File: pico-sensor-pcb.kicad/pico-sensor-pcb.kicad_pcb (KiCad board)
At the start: 2 copper layers, 46 x 60 mm, 38 parts, among them J1 Conn_PDM, J10 Conn_PCB_2, J11 Conn_I2C1, J13 Conn_I2C1, J2 Conn_RUN_ON, J3 Conn_Controls, J7 Conn_PCB_1, SW1 SW_Push, SW2 SW_Push, SW3 SW_Push, SW4 SW_Push, SW5 SW_Push, U1 AHT20, U2 BH1750FVI-TR, U3 SCD40_Breakout, U4 ENS160_Breakout

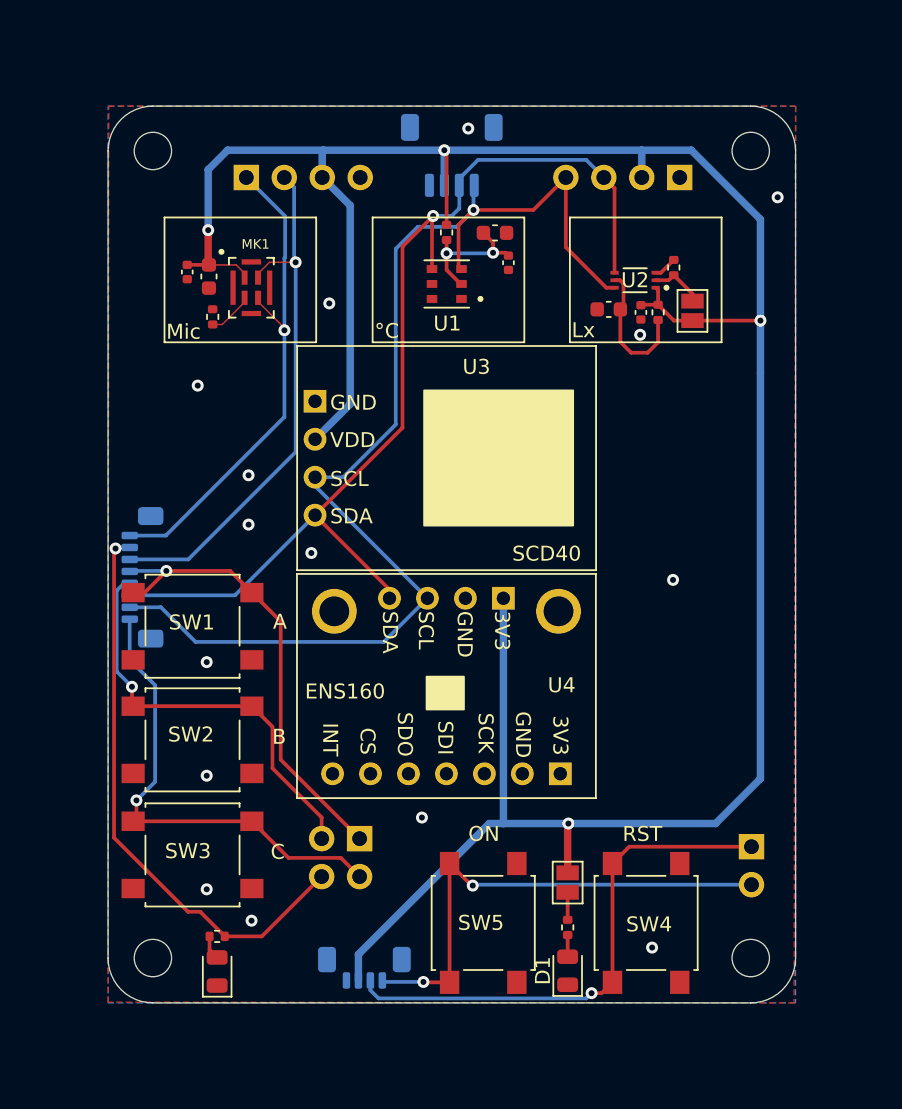
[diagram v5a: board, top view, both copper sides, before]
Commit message: Sensor-PCB Rev 1.95: larger PCB, I2C-pullups, labels (ready for review)
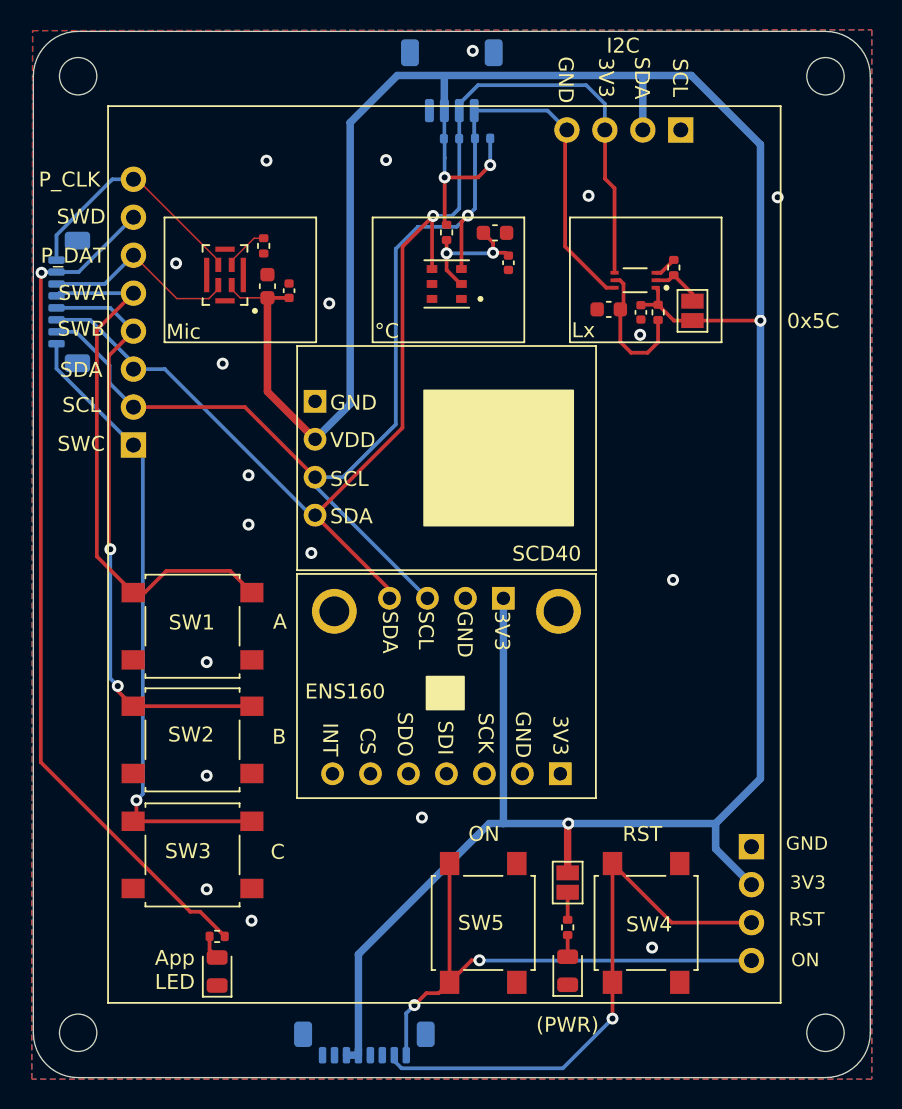
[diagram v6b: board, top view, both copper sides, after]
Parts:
- removed J3: Conn_Controls, Connector_PinHeader_2.54mm:PinHeader_2x02_P2.54mm_Vertical
- added R7: 10K, Resistor_SMD:R_0402_1005Metric, B.Cu at (125.1, 102.2)
- added R8: 10K, Resistor_SMD:R_0402_1005Metric, B.Cu at (123.0, 102.2)
- J1: value Conn_PDM -> THT_PCB2; footprint Connector_PinHeader_2.54mm:PinHeader_1x04_P2.54mm_Vertical -> Connector_PinHeader_2.54mm:PinHeader_1x08_P2.54mm_Vertical
- J10: value Conn_PCB_2 -> Conn_PCB2
- J2: footprint Connector_PinHeader_2.54mm:PinHeader_1x02_P2.54mm_Vertical -> Connector_PinHeader_2.54mm:PinHeader_1x04_P2.54mm_Vertical
- J7: footprint Connector_JST:JST_SUR_BM04B-SURS-TF_1x04-1MP_P0.80mm_Vertical -> Connector_JST:JST_SUR_BM08B-SURS-TF_1x08-1MP_P0.80mm_Vertical
- R5: value 150Ω -> 1K
- moved J1 19.4 mm to (101.7, 122.7), turned to 0 degrees
- moved J10 19.1 mm to (97.4, 113.1)
- moved H1 7.07 mm to (98.0, 98.0)
- moved H2 7.07 mm to (148.0, 98.0)
- moved H3 7.07 mm to (98.0, 162.0)
- moved H4 7.07 mm to (148.0, 162.0)
- moved C3 6.93 mm to (112.1, 112.3), turned to 90 degrees
- moved R2 5.85 mm to (110.4, 109.3), turned to 90 degrees
- moved J11 5.00 mm to (123.0, 98.3)
- moved J7 5.00 mm to (117.2, 162.7)
- moved C4 3.97 mm to (110.7, 112.0), turned to 90 degrees
- moved J13 3.18 mm to (138.3, 101.6)
- moved MK1 1.96 mm to (107.8, 111.3), turned to 180 degrees
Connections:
- J1 pad 1: /PDM_CLK -> /SWC
- J1 pad 2: /PDM_DAT -> /SCL
- J1 pad 3: +3V3 -> /SDA
- J1 pad 4: GND -> /SWB
- J2 pad 1: /RUN -> GND
- J2 pad 2: /~{ON} -> +3V3
- J7 pad 3: +3V3 -> unconnected-(J7-Pad3)
- J7 pad 4: GND -> unconnected-(J7-Pad4)
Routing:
- net /PDM_DAT: track 35.9 -> 13.0 mm, vias 1 -> 0
- net +3V3: track 179.6 -> 201.4 mm
- net /SWD: track 38.7 -> 57.6 mm
- net /SDA: track 70.4 -> 88.3 mm
- net /PDM_CLK: track 33.7 -> 16.3 mm, vias 1 -> 0
- net /SWB: track 28.0 -> 40.2 mm, vias 1 -> 2
- net /SWC: track 31.5 -> 42.6 mm
- net /SCL: track 80.4 -> 87.6 mm
- net /SWA: track 31.1 -> 36.4 mm, vias 1 -> 0
- net /RUN: track 35.2 -> 37.9 mm
- net /~{ON}: track 33.3 -> 35.3 mm
- net GND: track 1.57 -> 1.86 mm, vias 15 -> 19
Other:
- board size 46 x 60 mm -> 56 x 70 mm
- board text added: "(PWR)"
- board text added: "0x5C"
- board text added: "App LED"
- board text added: "I2C"
- board text added: "P_CLK"
- board text added: "P_DAT"
- board text added: "SWA"
- board text added: "SWB"
- board text added: "SWC"
- board text added: "SWD"
- board text added: "https://github.com/bablokb/pcb-pico-datalogger https://opendeved.net/ilce Rev 1.95"
- board text removed: "D"
- board text removed: "https://github.com/bablokb/pcb-pico-datalogger https://opendeved.net/ilce Rev 0.90"

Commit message: Sensor-PCB Rev 2.00: bump version to 2.00 (ready for production)
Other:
- board text added: "https://github.com/bablokb/pcb-pico-datalogger https://opendeved.net/ilce Rev 2.00"
- board text removed: "https://github.com/bablokb/pcb-pico-datalogger https://opendeved.net/ilce Rev 1.95"
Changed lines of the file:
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@@
     (property "Sheetname" "")
     (property "exclude_from_bom" "")
-    (attr through_hole exclude_from_bom)
+    (attr through_hole exclude_from_pos_files exclude_from_bom)
     (fp_text reference "J1" (at 0 2.33) (layer "B.SilkS") hide
       (effects (font (size 1 1) (thickness 0.15)) (justify mirror))
@@
     (property "Sheetname" "")
     (property "exclude_from_bom" "")
-    (attr through_hole exclude_from_bom)
+    (attr through_hole exclude_from_pos_files exclude_from_bom)
     (fp_text reference "J2" (at 0 2.33) (layer "B.SilkS") hide
       (effects (font (size 1 1) (thickness 0.15)) (justify mirror))
@@
     (pad "8" smd roundrect (at 2.8 -0.85 180) (size 0.5 1.1) (layers "B.Cu" "B.Paste" "B.Mask") (roundrect_rratio 0.25)
       (net 1 "GND") (pinfunction "Pin_8") (pintype "passive"))
-    (pad "MP" smd roundrect (at 4.1 0.55 180) (size 1.2 1.7) (layers "B.Cu" "B.Paste" "B.Mask") (roundrect_rratio 0.208333))
-    (pad "MP" smd roundrect (at -4.1 0.55 180) (size 1.2 1.7) (layers "B.Cu" "B.Paste" "B.Mask") (roundrect_rratio 0.208333))
+    (pad "MP" smd roundrect (at 4.1 0.55 180) (size 1.2 1.7) (layers "B.Cu" "B.Paste" "B.Mask") (roundrect_rratio 0.2083333333))
+    (pad "MP" smd roundrect (at -4.1 0.55 180) (size 1.2 1.7) (layers "B.Cu" "B.Paste" "B.Mask") (roundrect_rratio 0.2083333333))
     (model "${KICAD6_3DMODEL_DIR}/Connector_JST.3dshapes/JST_SUR_BM08B-SURS-TF_1x08-1MP_P0.80mm_Vertical.wrl"
       (offset (xyz 0 0 0))
@@
       (effects (font (size 1 1) (thickness 0.15)) (justify mirror))
     )
+    (fp_line (start 3.11 1.785) (end 2.06 1.785) (layer "B.SilkS") (width 0.12))
+    (fp_line (start -2.06 1.785) (end -2.06 2.775) (layer "B.SilkS") (width 0.12))
+    (fp_line (start -3.11 1.785) (end -2.06 1.785) (layer "B.SilkS") (width 0.12))
+    (fp_line (start 3.11 -0.715) (end 3.11 1.785) (layer "B.SilkS") (width 0.12))
+    (fp_line (start -3.11 -0.715) (end -3.11 1.785) (layer "B.SilkS") (width 0.12))
     (fp_line (start -1.94 -2.685) (end 1.94 -2.685) (layer "B.SilkS") (width 0.12))
-    (fp_line (start 3.11 -0.715) (end 3.11 1.785) (layer "B.SilkS") (width 0.12))
-    (fp_line (start -2.06 1.785) (end -2.06 2.775) (layer "B.SilkS") (width 0.12))
-    (fp_line (start -3.11 -0.715) (end -3.11 1.785) (layer "B.SilkS") (width 0.12))
-    (fp_line (start -3.11 1.785) (end -2.06 1.785) (layer "B.SilkS") (width 0.12))
-    (fp_line (start 3.11 1.785) (end 2.06 1.785) (layer "B.SilkS") (width 0.12))
+    (fp_line (start -3.9 3.28) (end -3.9 -3.28) (layer "B.CrtYd") (width 0.05))
     (fp_line (start -3.9 -3.28) (end 3.9 -3.28) (layer "B.CrtYd") (width 0.05))
     (fp_line (start 3.9 3.28) (end -3.9 3.28) (layer "B.CrtYd") (width 0.05))
     (fp_line (start 3.9 -3.28) (end 3.9 3.28) (layer "B.CrtYd") (width 0.05))
-    (fp_line (start -3.9 3.28) (end -3.9 -3.28) (layer "B.CrtYd") (width 0.05))
-    (fp_line (start -3 -2.575) (end 3 -2.575) (layer "B.Fab") (width 0.1))
-    (fp_line (start 3 1.675) (end 3 -2.575) (layer "B.Fab") (width 0.1))
     (fp_line (start -2 1.675) (end -1.5 0.967893) (layer "B.Fab") (width 0.1))
-    (fp_line (start -3 1.675) (end -3 -2.575) (layer "B.Fab") (width 0.1))
     (fp_line (start -3 1.675) (end 3 1.675) (layer "B.Fab") (width 0.1))
     (fp_line (start -1.5 0.967893) (end -1 1.675) (layer "B.Fab") (width 0.1))
+    (fp_line (start -3 1.675) (end -3 -2.575) (layer "B.Fab") (width 0.1))
+    (fp_line (start 3 1.675) (end 3 -2.575) (layer "B.Fab") (width 0.1))
+    (fp_line (start -3 -2.575) (end 3 -2.575) (layer "B.Fab") (width 0.1))
     (pad "1" smd roundrect (at -1.5 2) (size 0.6 1.55) (layers "B.Cu" "B.Paste" "B.Mask") (roundrect_rratio 0.25)
       (net 1 "GND") (pinfunction "GND") (pintype "power_in"))
@@
     (pad "4" smd roundrect (at 1.5 2) (size 0.6 1.55) (layers "B.Cu" "B.Paste" "B.Mask") (roundrect_rratio 0.25)
       (net 3 "/SCL") (pinfunction "SCL") (pintype "bidirectional"))
+    (pad "MP" smd roundrect (at -2.8 -1.875) (size 1.2 1.8) (layers "B.Cu" "B.Paste" "B.Mask") (roundrect_rratio 0.2083333333))
     (pad "MP" smd roundrect (at 2.8 -1.875) (size 1.2 1.8) (layers "B.Cu" "B.Paste" "B.Mask") (roundrect_rratio 0.2083333333))
-    (pad "MP" smd roundrect (at -2.8 -1.875) (size 1.2 1.8) (layers "B.Cu" "B.Paste" "B.Mask") (roundrect_rratio 0.2083333333))
     (model "${KICAD6_3DMODEL_DIR}/Connector_JST.3dshapes/JST_SH_SM04B-SRSS-TB_1x04-1MP_P1.00mm_Horizontal.wrl"
       (offset (xyz 0 0 0))
       (scale (xyz 1 1 1))
       (rotate (xyz 0 0 0))
+    )
+    (model "/home/bablokb/kicad/SM04B-SRSS-TB.step"
+      (offset (xyz 0 1.35 -0.35))
+      (scale (xyz 1 1 1))
+      (rotate (xyz -90 0 0))
     )
   )
@@
     (effects (font (size 1 1) (thickness 0.15)) (justify mirror))
   )
-  (gr_text "https://github.com/bablokb/pcb-pico-datalogger\nhttps://opendeved.net/ilce               Rev 1.95" (at 147.6 105.95 90) (layer "B.SilkS")
+  (gr_text "https://github.com/bablokb/pcb-pico-datalogger\nhttps://opendeved.net/ilce               Rev 2.00" (at 147.6 105.95 90) (layer "B.SilkS")
     (effects (font (size 1 1) (thickness 0.15)) (justify left mirror))
   )
